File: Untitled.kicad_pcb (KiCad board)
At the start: 2 copper layers, 0 parts

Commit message: Routed MCU
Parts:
- added C1: 0.1uF, Capacitor_SMD:C_0805_2012Metric, B.Cu at (61.9, 105.6)
- added C2: 0.1uF, Capacitor_SMD:C_0805_2012Metric, B.Cu at (57.9, 89.7)
- added C3: 22pF, Capacitor_SMD:C_0805_2012Metric, B.Cu at (69.1, 85.7)
- added C4: 22pF, Capacitor_SMD:C_0805_2012Metric, B.Cu at (61.1, 85.7)
- added C5: 0.1uF, Capacitor_SMD:C_0805_2012Metric, B.Cu at (75.9, 92.2)
- added C6: 0.1uF, Capacitor_SMD:C_0805_2012Metric, B.Cu at (68.9, 104.8)
- added C7: 1uF, Capacitor_SMD:C_0805_2012Metric, B.Cu at (56.4, 97.6)
- added D1: D_Small, Diode_SMD:D_SOD-123, B.Cu at (104.8, 88.9)
- added D2: D_Small, Diode_SMD:D_SOD-123, B.Cu at (131.0, 88.9)
- added D3: D_Small, Diode_SMD:D_SOD-123, B.Cu at (103.2, 108.0)
- added D4: D_Small, Diode_SMD:D_SOD-123, B.Cu at (131.0, 108.0)
- added F1: Polyfuse_Small, Fuse:Fuse_1206_3216Metric, B.Cu at (57.9, 111.9)
- added MX1: MX-NoLED, MX_Alps_Hybrid:MX-1.5U-NoLED, F.Cu at (93.7, 88.9)
- added MX2: MX-NoLED, MX_Alps_Hybrid:MX-1.5U-NoLED, F.Cu at (122.2, 88.9)
- added MX3: MX-NoLED, MX_Alps_Hybrid:MX-1.5U-NoLED, F.Cu at (93.7, 108.0)
- added MX4: MX-NoLED, MX_Alps_Hybrid:MX-1.5U-NoLED, F.Cu at (122.2, 108.0)
- added R1: 22, Resistor_SMD:R_0805_2012Metric, B.Cu at (51.6, 107.6)
- added R2: 22, Resistor_SMD:R_0805_2012Metric, B.Cu at (51.6, 109.5)
- added R3: 10k, Resistor_SMD:R_0805_2012Metric, B.Cu at (50.8, 94.5)
- added R4: 10k, Resistor_SMD:R_0805_2012Metric, B.Cu at (74.5, 103.8)
- added SW1: SW_Push, random-keyboard-parts:SKQG-1155865, B.Cu at (50.8, 88.9)
- added U1: ATmega32U4-AU, Package_QFP:TQFP-44_10x10mm_P0.8mm, B.Cu at (65.1, 96.8)
- added USB1: Molex-0548190589, random-keyboard-parts:Molex-0548190589, B.Cu at (50.0, 119.9)
- added Y1: 16MHz, Crystal:Crystal_SMD_3225-4Pin_3.2x2.5mm, B.Cu at (65.1, 85.7)
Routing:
- net GND: track 0.00 -> 123.9 mm, vias 0 -> 5
- net +5V: track 0.00 -> 74.5 mm, vias 0 -> 5
- net Net-(R3-Pad2): track 0.00 -> 16.8 mm
- net Net-(R2-Pad1): track 0.00 -> 16.6 mm
- net Net-(R1-Pad1): track 0.00 -> 13.5 mm
- net Net-(C4-Pad1): track 0.00 -> 10.3 mm
- net D-: track 0.00 -> 8.80 mm
- net VCC: track 0.00 -> 8.06 mm
- net Net-(C3-Pad1): track 0.00 -> 7.93 mm
- net D+: track 0.00 -> 6.83 mm
- net Net-(R4-Pad2): track 0.00 -> 4.58 mm
- net Net-(C7-Pad1): track 0.00 -> 3.10 mm
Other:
- net class Default: trace_width 0.25 -> 0.254
- net class Power added: clearance 0.2, trace_width 0.381, via_dia 0.8, via_drill 0.4

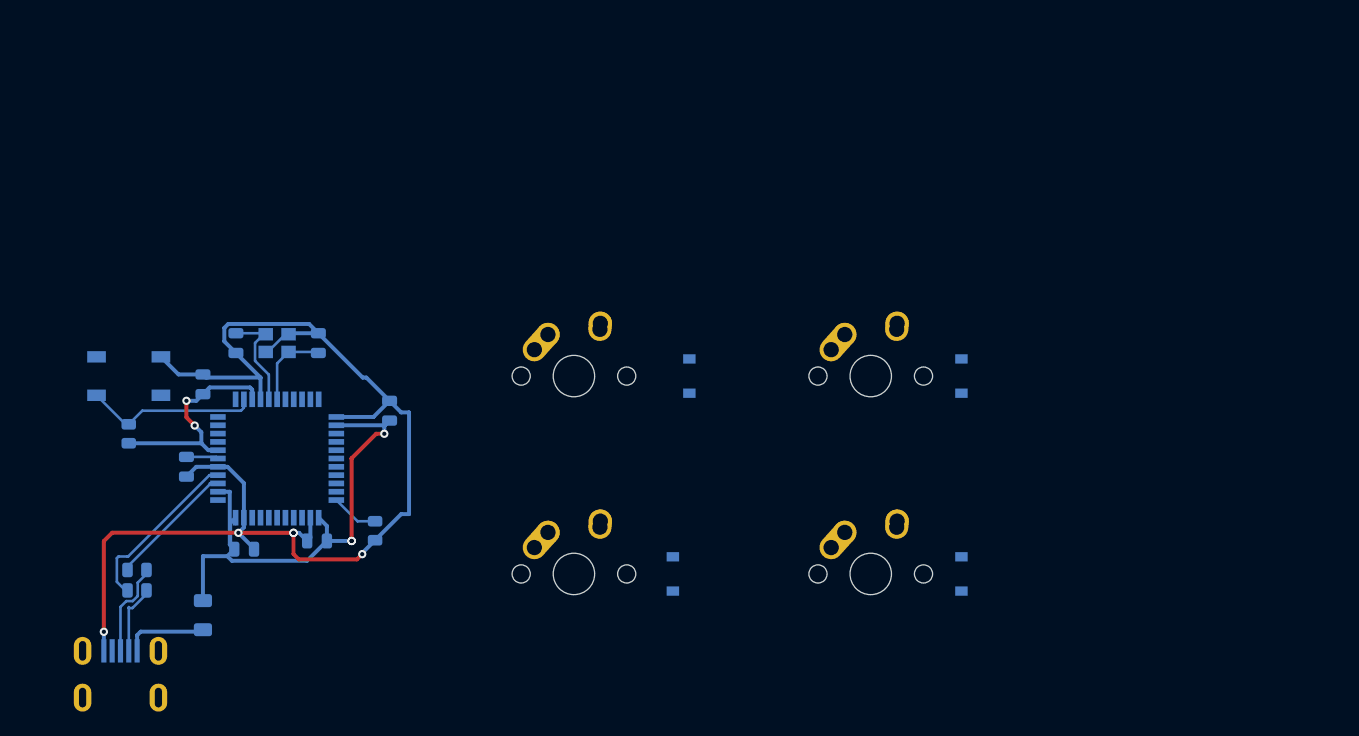
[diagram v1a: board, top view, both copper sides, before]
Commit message: Keyboard  - ICSP  - Fixed USB D+/D-
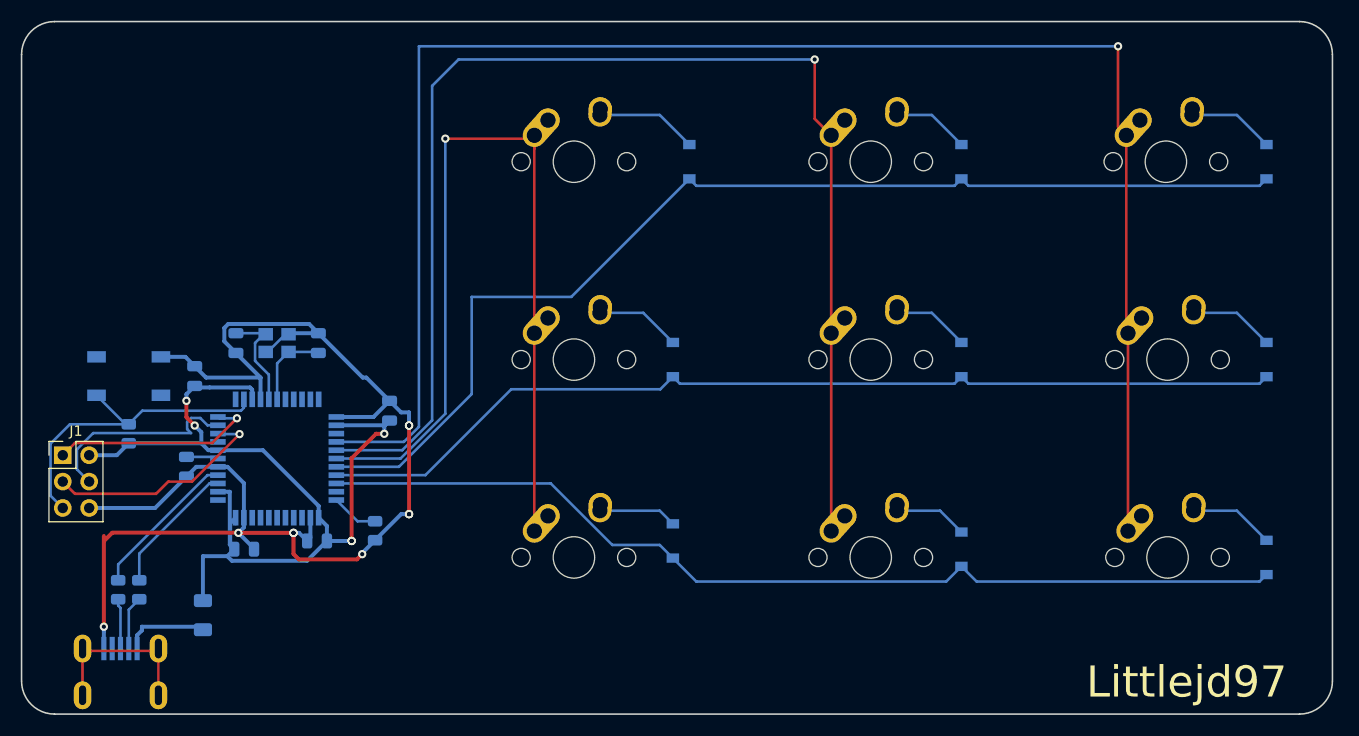
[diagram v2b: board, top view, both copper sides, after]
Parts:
- added D5: D_Small, Diode_SMD:D_SOD-123, B.Cu at (103.2, 104.8)
- added D6: D_Small, Diode_SMD:D_SOD-123, B.Cu at (131.0, 105.6)
- added D7: D_Small, Diode_SMD:D_SOD-123, B.Cu at (160.3, 87.3)
- added D8: D_Small, Diode_SMD:D_SOD-123, B.Cu at (160.3, 106.4)
- added D9: D_Small, Diode_SMD:D_SOD-123, B.Cu at (160.3, 68.3)
- added J1: Conn_02x03_Odd_Even, Connector_PinHeader_2.54mm:PinHeader_2x03_P2.54mm_Vertical, F.Cu at (44.5, 96.5)
- added MX5: MX-NoLED, MX_Alps_Hybrid:MX-1.5U-NoLED, F.Cu at (93.7, 106.4)
- added MX6: MX-NoLED, MX_Alps_Hybrid:MX-1.5U-NoLED, F.Cu at (122.2, 106.4)
- added MX7: MX-NoLED, MX_Alps_Hybrid:MX-1.5U-NoLED, F.Cu at (150.8, 87.3)
- added MX8: MX-NoLED, MX_Alps_Hybrid:MX-1.5U-NoLED, F.Cu at (150.8, 106.4)
- added MX9: MX-NoLED, MX_Alps_Hybrid:MX-1.5U-NoLED, F.Cu at (150.7, 68.3)
- C6: value 0.1uF -> 10uF
- moved D1 20.6 mm to (104.8, 68.3)
- moved D2 20.6 mm to (131.0, 68.3)
- moved D3 20.6 mm to (103.2, 87.3)
- moved D4 20.6 mm to (131.0, 87.3)
- moved MX1 20.6 mm to (93.7, 68.3)
- moved MX2 20.6 mm to (122.2, 68.3)
- moved MX3 20.6 mm to (93.7, 87.3)
- moved MX4 20.6 mm to (122.2, 87.3)
- moved R1 1.92 mm to (51.8, 109.5), turned to 270 degrees
- moved R2 1.81 mm to (49.8, 109.5), turned to 270 degrees
- moved C2 1.12 mm to (57.1, 88.9)
- moved USB1 0.22 mm to (50.0, 119.6)
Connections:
- U1 pad 26: Net-(U1-Pad26) -> COL2
- U1 pad 27: Net-(U1-Pad27) -> COL1
- U1 pad 28: Net-(U1-Pad28) -> COL0
- U1 pad 29: Net-(U1-Pad29) -> ROW0
- U1 pad 30: Net-(U1-Pad30) -> ROW1
- U1 pad 31: Net-(U1-Pad31) -> ROW2
- USB1 pad 3: D- -> D+
- USB1 pad 4: D+ -> D-
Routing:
- net COL2: track 0.00 -> 160.8 mm, vias 0 -> 1
- net COL1: track 0.00 -> 126.6 mm, vias 0 -> 1
- net ROW0: track 0.00 -> 107.6 mm
- net ROW2: track 0.00 -> 95.0 mm
- net ROW1: track 0.00 -> 94.6 mm
- net COL0: track 0.00 -> 87.5 mm, vias 0 -> 1
- net Net-(J1-Pad3): track 0.00 -> 22.0 mm, vias 0 -> 1
- net Net-(J1-Pad1): track 0.00 -> 20.1 mm, vias 0 -> 1
- net Net-(J1-Pad4): track 0.00 -> 19.9 mm
- net +5V: track 74.5 -> 92.3 mm
- net Net-(USB1-Pad6): track 0.00 -> 16.3 mm
- net Net-(J1-Pad5): track 16.8 -> 31.8 mm
- net GND: track 123.9 -> 135.2 mm, vias 5 -> 9
- net Net-(D1-Pad2): track 0.00 -> 9.79 mm
- net Net-(D9-Pad2): track 0.00 -> 8.96 mm
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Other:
- board outline added: 126.2 x 66.7 mm
- rule via_min_size: 0.4 -> 0
- board text added: "Littlejd97"
